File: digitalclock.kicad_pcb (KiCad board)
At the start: 4 copper layers, 82 x 65 mm, 98 parts, among them J2 MEM2075-00-140-01-A, J3 Conn_01x12_Socket, J4 Conn_01x05, J5 Conn_01x07_Socket, J6 Conn_01x07_Socket, J7 Conn_01x07_Socket, J8 Conn_01x07_Socket, Q1 DMP2070UQ-7, Q2 MMBT2222A-7-F, SW1 KMR2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

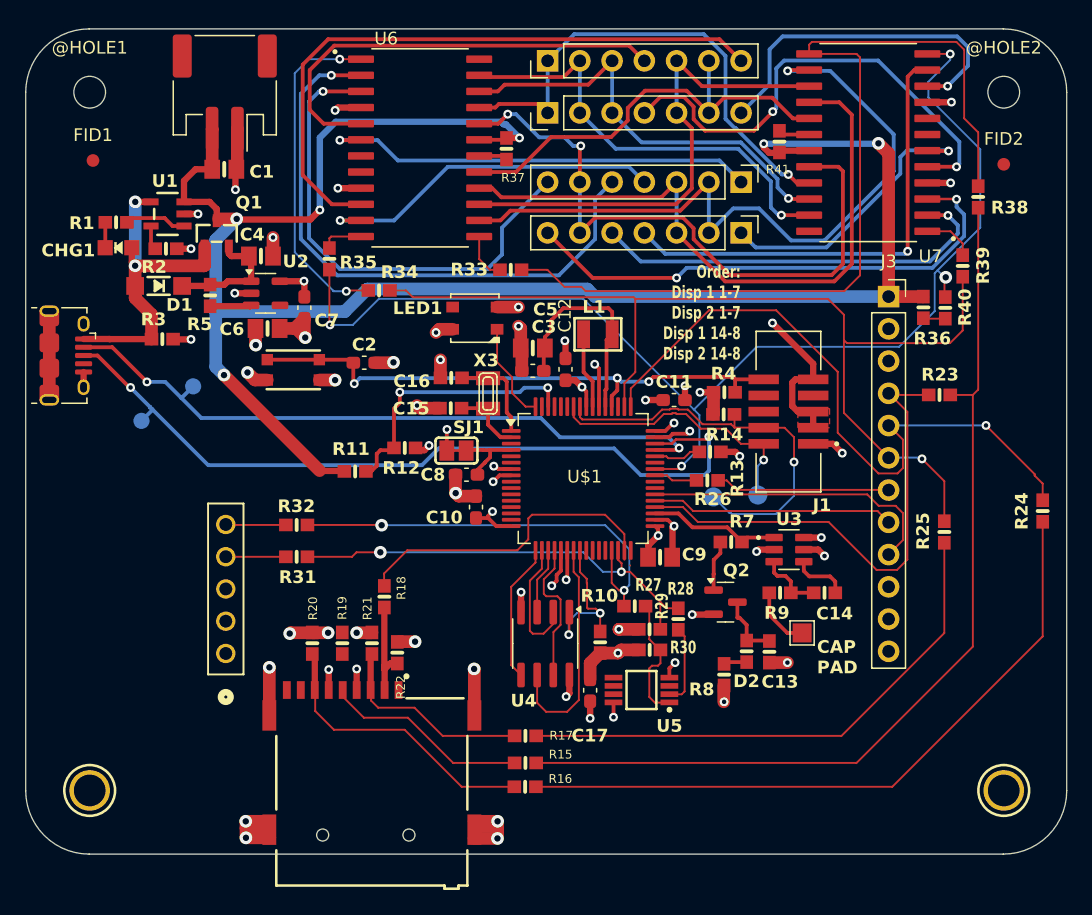
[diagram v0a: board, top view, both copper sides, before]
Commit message: Updated BOM, created fab outputs
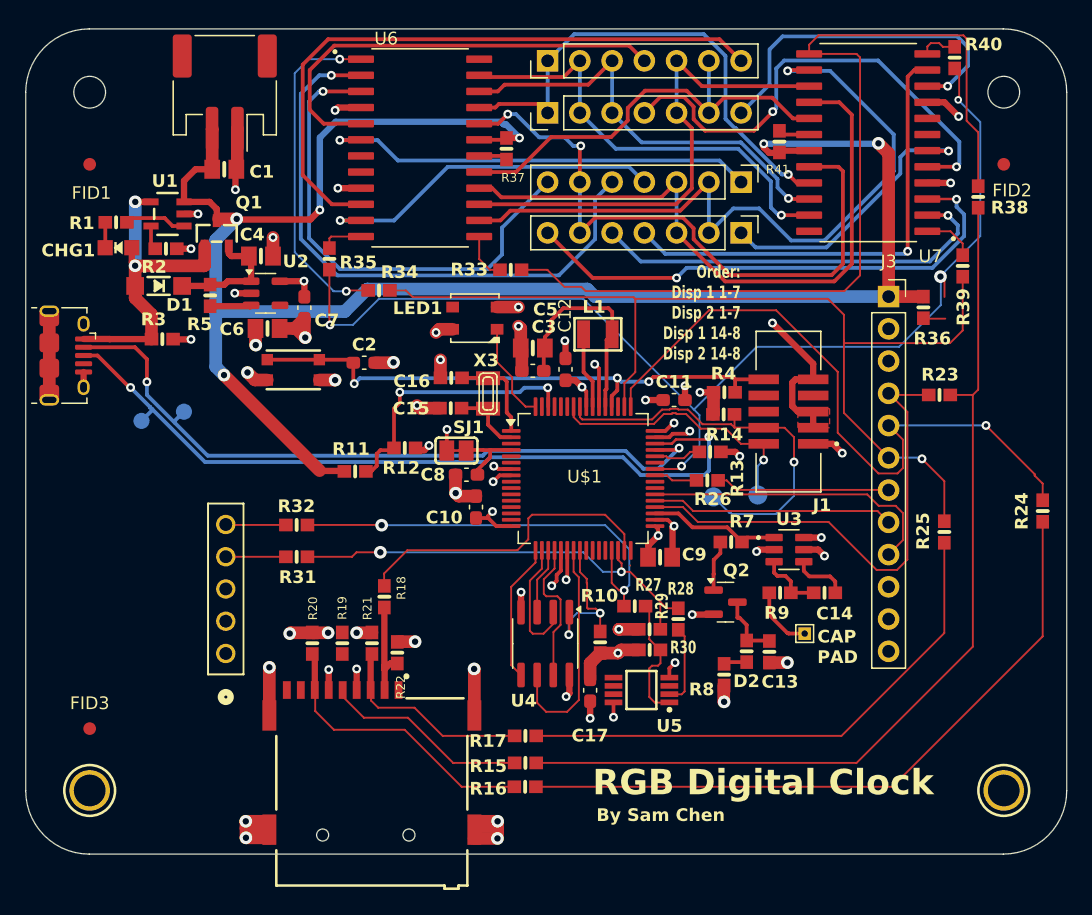
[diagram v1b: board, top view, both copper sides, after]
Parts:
- added FID3: Fiducial, Fiducial:Fiducial_1mm_Mask2mm, F.Cu at (117.7, 116.2)
- TP1: footprint TestPoint:TestPoint_Pad_1.5x1.5mm -> TestPoint:TestPoint_THTPad_1.0x1.0mm_Drill0.5mm
- moved R40 19.7 mm to (185.9, 63.3)
- moved TP3 2.12 mm to (125.1, 91.2)
- moved FID1 0.40 mm to (117.7, 71.8)
- moved TP1 0.21 mm to (174.0, 108.7)
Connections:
- SJ1 pad WIRE: +3V3 -> (no net)
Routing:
- net /D-: track 53.5 -> 56.6 mm
- net /CS3: track 100.5 -> 98.7 mm
- net /SCLK: track 206.8 -> 207.9 mm
- net GND: track 111.0 -> 112.0 mm
- net /D+: track 62.9 -> 62.1 mm
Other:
- board text added: "2"
- board text added: "3"
- board text added: "3V3"
- board text added: "By Sam Chen"
- board text added: "GND"
- board text added: "RGB Digital Clock"

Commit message: Final project submission
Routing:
- net /CS3: track 98.7 -> 99.4 mm
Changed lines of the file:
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@@
 	)
 	(segment
-		(start 184.7342 80.5942)
-		(end 185.05 80.91)
+		(start 185.05 82.2832)
+		(end 183.4252 83.908)
+		(width 0.15)
+		(layer "F.Cu")
+		(net 105)
+	)
+	(segment
+		(start 185.05 80.91)
+		(end 185.05 82.2832)
 		(width 0.15)
 		(layer "F.Cu")
@@
 	)
 	(segment
-		(start 185.1152 83.908)
-		(end 183.4252 83.908)
-		(width 0.15)
-		(layer "F.Cu")
-		(net 105)
-	)
-	(segment
 		(start 136.6012 80.0472)
 		(end 136.6012 84.3512)
@@
 		(start 136.7328 77.44)
 		(end 136.6012 77.5716)
+		(width 0.15)
+		(layer "F.Cu")
+		(net 105)
+	)
+	(segment
+		(start 184.7342 80.5942)
+		(end 185.05 80.91)
 		(width 0.15)
 		(layer "F.Cu")
@@
 		(width 0.15)
 		(layer "F.Cu")
-		(net 105)
-	)
-	(segment
-		(start 185.05 80.91)
-		(end 185.05 82.2)
-		(width 0.15)
-		(layer "F.Cu")
